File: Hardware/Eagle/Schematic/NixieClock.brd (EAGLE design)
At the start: 256.5 x 112.7 mm, 10 parts

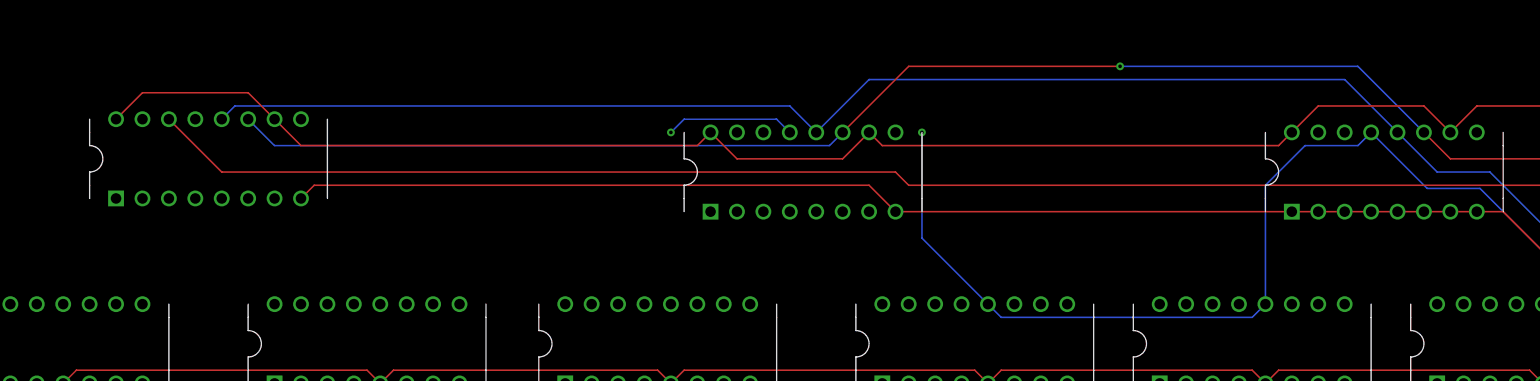
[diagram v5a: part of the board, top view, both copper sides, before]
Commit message: Schematic progress... chips in board layout are out of order.. fix later
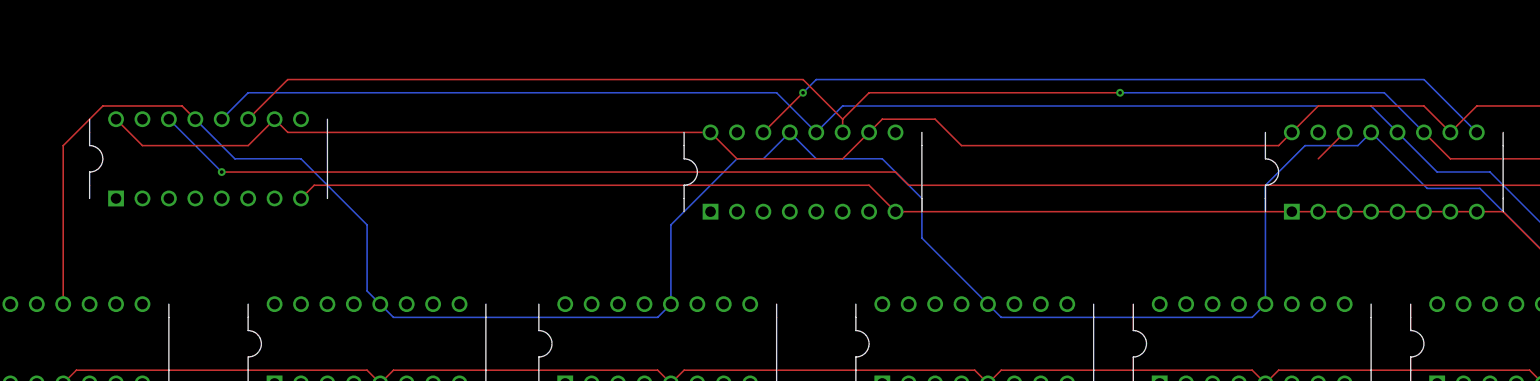
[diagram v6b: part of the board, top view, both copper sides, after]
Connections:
- new net N$7: U$2.P$9, U$3.P$14
- new net N$9: U$3.P$9, U$4.P$14
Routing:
- net N$1: track 156.7 -> 263.8 mm, vias 2 -> 0
- net N$9: track 0.00 -> 72.8 mm, vias 0 -> 1
- net N$7: track 0.00 -> 3.59 mm
- net N$5: track 169.1 -> 168.1 mm
- net N$3: vias 0 -> 1
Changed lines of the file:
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@@
 <wire x1="34.29" y1="43.18" x2="33.02" y2="44.45" width="0.1524" layer="16"/>
 <wire x1="33.02" y1="44.45" x2="26.67" y2="50.8" width="0.1524" layer="16"/>
-<wire x1="26.67" y1="50.8" x2="26.67" y2="60.96" width="0.1524" layer="16"/>
-<via x="26.67" y="60.96" extent="1-16" drill="0.35"/>
-<wire x1="13.97" y1="60.96" x2="12.7" y2="62.23" width="0.1524" layer="16"/>
-<wire x1="12.7" y1="62.23" x2="3.81" y2="62.23" width="0.1524" layer="16"/>
-<wire x1="3.81" y1="62.23" x2="2.54" y2="60.96" width="0.1524" layer="16"/>
-<via x="2.54" y="60.96" extent="1-16" drill="0.35"/>
-<wire x1="13.97" y1="60.96" x2="26.67" y2="60.96" width="0" layer="19" extent="1-1"/>
-<wire x1="2.54" y1="44.45" x2="2.54" y2="60.96" width="0" layer="19" extent="1-1"/>
-<wire x1="-25.4" y1="44.45" x2="2.54" y2="44.45" width="0" layer="19" extent="1-1"/>
-<wire x1="-43.18" y1="62.23" x2="-25.4" y2="44.45" width="0" layer="19" extent="1-1"/>
-<wire x1="-55.88" y1="44.45" x2="-43.18" y2="62.23" width="0" layer="19" extent="1-1"/>
+<wire x1="13.97" y1="60.96" x2="11.43" y2="58.42" width="0.1524" layer="16"/>
+<wire x1="11.43" y1="58.42" x2="8.89" y2="58.42" width="0.1524" layer="16"/>
+<wire x1="8.89" y1="58.42" x2="2.54" y2="52.07" width="0.1524" layer="16"/>
+<wire x1="2.54" y1="52.07" x2="2.54" y2="44.45" width="0.1524" layer="16"/>
+<wire x1="26.67" y1="50.8" x2="26.67" y2="54.61" width="0.1524" layer="16"/>
+<wire x1="26.67" y1="54.61" x2="22.86" y2="58.42" width="0.1524" layer="16"/>
+<wire x1="22.86" y1="58.42" x2="16.51" y2="58.42" width="0.1524" layer="16"/>
+<wire x1="16.51" y1="58.42" x2="13.97" y2="60.96" width="0.1524" layer="16"/>
+<wire x1="-43.18" y1="62.23" x2="-39.37" y2="58.42" width="0.1524" layer="16"/>
+<wire x1="-39.37" y1="58.42" x2="-33.02" y2="58.42" width="0.1524" layer="16"/>
+<wire x1="-33.02" y1="58.42" x2="-26.67" y2="52.07" width="0.1524" layer="16"/>
+<wire x1="-26.67" y1="52.07" x2="-26.67" y2="45.72" width="0.1524" layer="16"/>
+<wire x1="-26.67" y1="45.72" x2="-25.4" y2="44.45" width="0.1524" layer="16"/>
+<wire x1="-25.4" y1="44.45" x2="-24.13" y2="43.18" width="0.1524" layer="16"/>
+<wire x1="1.27" y1="43.18" x2="2.54" y2="44.45" width="0.1524" layer="16"/>
+<wire x1="-24.13" y1="43.18" x2="1.27" y2="43.18" width="0.1524" layer="16"/>
+<wire x1="-43.18" y1="62.23" x2="-44.45" y2="63.5" width="0.1524" layer="1"/>
+<wire x1="-44.45" y1="63.5" x2="-52.07" y2="63.5" width="0.1524" layer="1"/>
+<wire x1="-55.88" y1="59.69" x2="-55.88" y2="44.45" width="0.1524" layer="1"/>
+<wire x1="-52.07" y1="63.5" x2="-55.88" y2="59.69" width="0.1524" layer="1"/>
 </signal>
 <signal name="N$2">
@@
 <wire x1="64.77" y1="63.5" x2="62.23" y2="60.96" width="0.1524" layer="1"/>
 <wire x1="62.23" y1="60.96" x2="60.96" y2="59.69" width="0.1524" layer="1"/>
-<wire x1="60.96" y1="59.69" x2="22.86" y2="59.69" width="0.1524" layer="1"/>
-<wire x1="22.86" y1="59.69" x2="21.59" y2="60.96" width="0.1524" layer="1"/>
-<wire x1="6.35" y1="60.96" x2="5.08" y2="59.69" width="0.1524" layer="1"/>
-<wire x1="5.08" y1="59.69" x2="-33.02" y2="59.69" width="0.1524" layer="1"/>
-<wire x1="-33.02" y1="59.69" x2="-35.56" y2="62.23" width="0.1524" layer="1"/>
-<wire x1="-35.56" y1="62.23" x2="-38.1" y2="64.77" width="0.1524" layer="1"/>
-<wire x1="-38.1" y1="64.77" x2="-48.26" y2="64.77" width="0.1524" layer="1"/>
-<wire x1="-48.26" y1="64.77" x2="-50.8" y2="62.23" width="0.1524" layer="1"/>
+<wire x1="60.96" y1="59.69" x2="30.48" y2="59.69" width="0.1524" layer="1"/>
+<wire x1="30.48" y1="59.69" x2="27.94" y2="62.23" width="0.1524" layer="1"/>
+<wire x1="27.94" y1="62.23" x2="22.86" y2="62.23" width="0.1524" layer="1"/>
+<wire x1="22.86" y1="62.23" x2="21.59" y2="60.96" width="0.1524" layer="1"/>
+<wire x1="6.35" y1="60.96" x2="-34.29" y2="60.96" width="0.1524" layer="1"/>
+<wire x1="-34.29" y1="60.96" x2="-35.56" y2="62.23" width="0.1524" layer="1"/>
+<wire x1="-35.56" y1="62.23" x2="-38.1" y2="59.69" width="0.1524" layer="1"/>
+<wire x1="-50.8" y1="62.23" x2="-48.26" y2="59.69" width="0.1524" layer="1"/>
+<wire x1="-38.1" y1="59.69" x2="-48.26" y2="59.69" width="0.1524" layer="1"/>
 <wire x1="6.35" y1="60.96" x2="8.89" y2="58.42" width="0.1524" layer="1"/>
 <wire x1="21.59" y1="60.96" x2="19.05" y2="58.42" width="0.1524" layer="1"/>
@@
 <wire x1="25.401325" y1="55.878675" x2="24.13" y2="57.15" width="0.1524" layer="1"/>
 <wire x1="24.13" y1="57.15" x2="-40.64" y2="57.15" width="0.1524" layer="1"/>
-<wire x1="-40.64" y1="57.15" x2="-45.72" y2="62.23" width="0.1524" layer="1"/>
 <wire x1="86.361325" y1="55.878675" x2="87.7822" y2="54.4578" width="0.1524" layer="1"/>
 <wire x1="87.7822" y1="54.4578" x2="110.3378" y2="54.4578" width="0.1524" layer="1"/>
+<via x="-40.64" y="57.15" extent="1-16" drill="0.35"/>
+<wire x1="-40.64" y1="57.15" x2="-45.72" y2="62.23" width="0.1524" layer="16"/>
 </signal>
 <signal name="N$4">
@@
 <wire x1="86.36" y1="58.42" x2="77.47" y2="58.42" width="0.1524" layer="1"/>
 <wire x1="77.47" y1="58.42" x2="74.93" y2="60.96" width="0.1524" layer="1"/>
-<wire x1="74.93" y1="60.96" x2="68.58" y2="67.31" width="0.1524" layer="16"/>
-<wire x1="68.58" y1="67.31" x2="45.72" y2="67.31" width="0.1524" layer="16"/>
-<wire x1="19.05" y1="60.96" x2="17.78" y2="59.69" width="0.1524" layer="16"/>
-<wire x1="-38.1" y1="62.23" x2="-35.56" y2="59.69" width="0.1524" layer="16"/>
-<wire x1="17.78" y1="59.69" x2="-35.56" y2="59.69" width="0.1524" layer="16"/>
-<via x="45.72" y="67.31" extent="1-16" drill="0.35"/>
-<wire x1="45.72" y1="67.31" x2="25.4" y2="67.31" width="0.1524" layer="1"/>
-<wire x1="25.4" y1="67.31" x2="19.05" y2="60.96" width="0.1524" layer="1"/>
+<wire x1="74.93" y1="60.96" x2="71.12" y2="64.77" width="0.1524" layer="16"/>
+<wire x1="71.12" y1="64.77" x2="45.72" y2="64.77" width="0.1524" layer="16"/>
+<via x="45.72" y="64.77" extent="1-16" drill="0.35"/>
+<wire x1="45.72" y1="64.77" x2="21.59" y2="64.77" width="0.1524" layer="1"/>
+<wire x1="21.59" y1="64.77" x2="19.05" y2="62.23" width="0.1524" layer="1"/>
+<wire x1="19.05" y1="60.96" x2="19.05" y2="62.23" width="0.1524" layer="1"/>
+<wire x1="19.05" y1="62.23" x2="15.24" y2="66.04" width="0.1524" layer="1"/>
+<wire x1="-34.29" y1="66.04" x2="15.24" y2="66.04" width="0.1524" layer="1"/>
+<wire x1="-38.1" y1="62.23" x2="-34.29" y2="66.04" width="0.1524" layer="1"/>
 </signal>
 <signal name="N$5">
@@
 <wire x1="81.28" y1="57.15" x2="76.2" y2="57.15" width="0.1524" layer="16"/>
 <wire x1="76.2" y1="57.15" x2="72.39" y2="60.96" width="0.1524" layer="16"/>
-<wire x1="72.39" y1="60.96" x2="67.31" y2="66.04" width="0.1524" layer="16"/>
-<wire x1="21.59" y1="66.04" x2="16.51" y2="60.96" width="0.1524" layer="16"/>
-<wire x1="67.31" y1="66.04" x2="21.59" y2="66.04" width="0.1524" layer="16"/>
-<wire x1="-40.64" y1="62.23" x2="-39.37" y2="63.5" width="0.1524" layer="16"/>
-<wire x1="16.51" y1="60.96" x2="13.97" y2="63.5" width="0.1524" layer="16"/>
-<wire x1="13.97" y1="63.5" x2="-39.37" y2="63.5" width="0.1524" layer="16"/>
+<wire x1="72.39" y1="60.96" x2="69.85" y2="63.5" width="0.1524" layer="16"/>
+<wire x1="19.05" y1="63.5" x2="16.51" y2="60.96" width="0.1524" layer="16"/>
+<wire x1="69.85" y1="63.5" x2="19.05" y2="63.5" width="0.1524" layer="16"/>
+<wire x1="-40.64" y1="62.23" x2="-38.1" y2="64.77" width="0.1524" layer="16"/>
+<wire x1="16.51" y1="60.96" x2="12.7" y2="64.77" width="0.1524" layer="16"/>
+<wire x1="12.7" y1="64.77" x2="-38.1" y2="64.77" width="0.1524" layer="16"/>
 </signal>
 <signal name="N$6">
@@
 <wire x1="-54.61" y1="38.1" x2="-55.88" y2="36.83" width="0.1524" layer="1"/>
 </signal>
+<signal name="N$7">
+<contactref element="U$2" pad="P$9"/>
+<contactref element="U$3" pad="P$14"/>
+<wire x1="67.31" y1="60.96" x2="64.77" y2="58.42" width="0.1524" layer="1"/>
+<wire x1="-33.02" y1="62.23" x2="64.77" y2="58.42" width="0" layer="19" extent="1-1"/>
+</signal>
+<signal name="N$9">
+<contactref element="U$3" pad="P$9"/>
+<contactref element="U$4" pad="P$14"/>
+<wire x1="80.01" y1="60.96" x2="74.93" y2="66.04" width="0.1524" layer="16"/>
+<wire x1="16.51" y1="66.04" x2="15.24" y2="64.77" width="0.1524" layer="16"/>
+<wire x1="74.93" y1="66.04" x2="16.51" y2="66.04" width="0.1524" layer="16"/>
+<via x="15.24" y="64.77" extent="1-16" drill="0.35"/>
+<wire x1="15.24" y1="64.77" x2="11.43" y2="60.96" width="0.1524" layer="1"/>
+</signal>
 </signals>

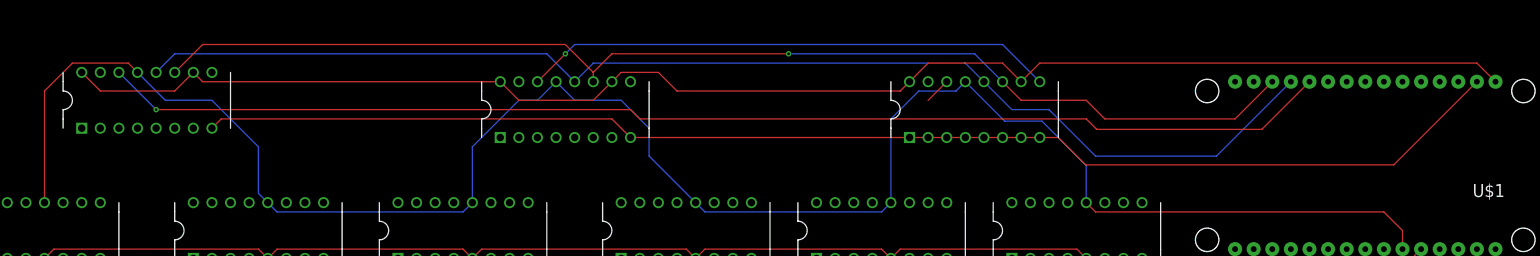
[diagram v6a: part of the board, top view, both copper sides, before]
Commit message: Chips in board layout in correct order
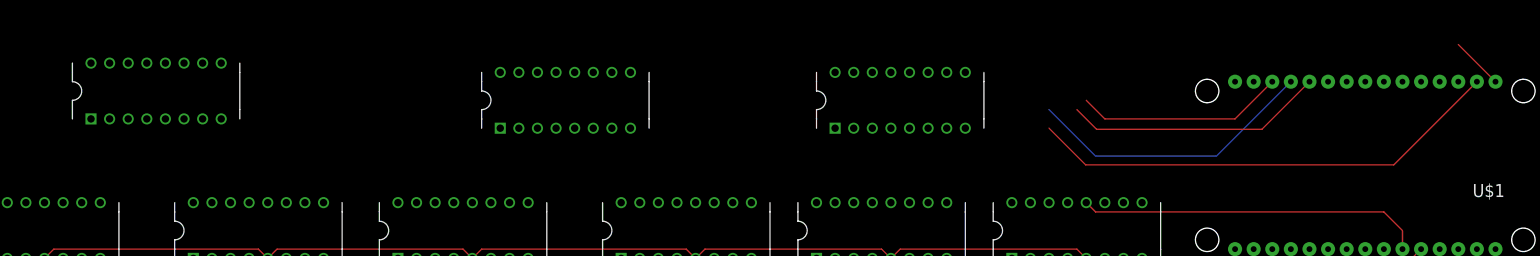
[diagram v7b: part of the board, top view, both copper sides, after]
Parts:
- moved U$2 102.9 mm to (61.0, 58.4)
- moved U$4 55.9 mm to (-40.6, 59.7)
- moved U$3 55.9 mm to (15.2, 58.4)
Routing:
- net N$1: track 263.8 -> 47.3 mm
- net N$2: track 204.1 -> 7.18 mm
- net N$3: track 168.5 -> 35.6 mm, vias 1 -> 0
- net N$4: track 161.1 -> 28.6 mm, vias 1 -> 0
- net N$5: track 168.1 -> 39.9 mm
- net N$6: track 180.5 -> 65.2 mm
- net N$9: track 72.8 -> 0.00 mm, vias 1 -> 0
- net N$7: track 3.59 -> 0.00 mm

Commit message: All wires from shift registers to nixie driver inputs routed
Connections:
- new net N$10: U$10.P$3, U$2.P$7
- new net N$11: U$3.P$7, U$8.P$3
- new net N$12: U$4.P$7, U$6.P$3
- new net N$13: U$10.P$6, U$2.P$6
- new net N$14: U$3.P$6, U$8.P$6
- new net N$15: U$4.P$6, U$6.P$6
- new net N$16: U$10.P$7, U$2.P$5
- new net N$17: U$3.P$5, U$8.P$7
- new net N$18: U$4.P$5, U$6.P$7
- new net N$19: U$10.P$4, U$2.P$4
- new net N$20: U$3.P$4, U$8.P$4
- new net N$21: U$4.P$4, U$6.P$4
- new net N$22: U$2.P$3, U$9.P$3
- new net N$23: U$3.P$3, U$7.P$3
- new net N$24: U$4.P$3, U$5.P$3
- new net N$25: U$2.P$2, U$9.P$6
- new net N$26: U$3.P$2, U$7.P$6
- new net N$27: U$4.P$2, U$5.P$6
- new net N$28: U$2.P$1, U$9.P$7
- new net N$29: U$3.P$1, U$7.P$7
- new net N$30: U$4.P$1, U$5.P$7
- new net N$31: U$4.P$15, U$5.P$4
- new net N$32: U$3.P$15, U$7.P$4
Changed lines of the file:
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@@
 <wire x1="-44.45" y1="63.5" x2="24.13" y2="62.23" width="0" layer="19" extent="1-1"/>
+</signal>
+<signal name="N$10">
+<contactref element="U$2" pad="P$7"/>
+<contactref element="U$10" pad="P$3"/>
+<wire x1="81.28" y1="36.83" x2="67.31" y2="54.61" width="0" layer="19" extent="1-1"/>
+</signal>
+<signal name="N$11">
+<contactref element="U$3" pad="P$7"/>
+<contactref element="U$8" pad="P$3"/>
+<wire x1="27.94" y1="36.83" x2="21.59" y2="54.61" width="0" layer="19" extent="1-1"/>
+</signal>
+<signal name="N$12">
+<contactref element="U$4" pad="P$7"/>
+<contactref element="U$6" pad="P$3"/>
+<wire x1="-30.48" y1="36.83" x2="-34.29" y2="55.88" width="0" layer="19" extent="1-1"/>
+</signal>
+<signal name="N$13">
+<contactref element="U$2" pad="P$6"/>
+<contactref element="U$10" pad="P$6"/>
+<wire x1="64.77" y1="54.61" x2="88.9" y2="36.83" width="0" layer="19" extent="1-1"/>
+</signal>
+<signal name="N$14">
+<contactref element="U$3" pad="P$6"/>
+<contactref element="U$8" pad="P$6"/>
+<wire x1="35.56" y1="36.83" x2="19.05" y2="54.61" width="0" layer="19" extent="1-1"/>
+</signal>
+<signal name="N$15">
+<contactref element="U$4" pad="P$6"/>
+<contactref element="U$6" pad="P$6"/>
+<wire x1="-22.86" y1="36.83" x2="-36.83" y2="55.88" width="0" layer="19" extent="1-1"/>
+</signal>
+<signal name="N$16">
+<contactref element="U$2" pad="P$5"/>
+<contactref element="U$10" pad="P$7"/>
+<wire x1="62.23" y1="54.61" x2="91.44" y2="36.83" width="0" layer="19" extent="1-1"/>
+</signal>
+<signal name="N$17">
+<contactref element="U$3" pad="P$5"/>
+<contactref element="U$8" pad="P$7"/>
+<wire x1="16.51" y1="54.61" x2="38.1" y2="36.83" width="0" layer="19" extent="1-1"/>
+</signal>
+<signal name="N$18">
+<contactref element="U$4" pad="P$5"/>
+<contactref element="U$6" pad="P$7"/>
+<wire x1="-20.32" y1="36.83" x2="-39.37" y2="55.88" width="0" layer="19" extent="1-1"/>
+</signal>
+<signal name="N$19">
+<contactref element="U$2" pad="P$4"/>
+<contactref element="U$10" pad="P$4"/>
+<wire x1="59.69" y1="54.61" x2="83.82" y2="36.83" width="0" layer="19" extent="1-1"/>
+</signal>
+<signal name="N$20">
+<contactref element="U$3" pad="P$4"/>
+<contactref element="U$8" pad="P$4"/>
+<wire x1="30.48" y1="36.83" x2="13.97" y2="54.61" width="0" layer="19" extent="1-1"/>
+</signal>
+<signal name="N$21">
+<contactref element="U$4" pad="P$4"/>
+<contactref element="U$6" pad="P$4"/>
+<wire x1="-27.94" y1="36.83" x2="-41.91" y2="55.88" width="0" layer="19" extent="1-1"/>
+</signal>
+<signal name="N$22">
+<contactref element="U$2" pad="P$3"/>
+<contactref element="U$9" pad="P$3"/>
+<wire x1="54.61" y1="36.83" x2="57.15" y2="54.61" width="0" layer="19" extent="1-1"/>
+</signal>
+<signal name="N$23">
+<contactref element="U$3" pad="P$3"/>
+<contactref element="U$7" pad="P$3"/>
+<wire x1="-2.54" y1="36.83" x2="11.43" y2="54.61" width="0" layer="19" extent="1-1"/>
+</signal>
+<signal name="N$24">
+<contactref element="U$4" pad="P$3"/>
+<contactref element="U$5" pad="P$3"/>
+<wire x1="-44.45" y1="55.88" x2="-60.96" y2="36.83" width="0" layer="19" extent="1-1"/>
+</signal>
+<signal name="N$25">
+<contactref element="U$2" pad="P$2"/>
+<contactref element="U$9" pad="P$6"/>
+<wire x1="62.23" y1="36.83" x2="54.61" y2="54.61" width="0" layer="19" extent="1-1"/>
+</signal>
+<signal name="N$26">
+<contactref element="U$3" pad="P$2"/>
+<contactref element="U$7" pad="P$6"/>
+<wire x1="5.08" y1="36.83" x2="8.89" y2="54.61" width="0" layer="19" extent="1-1"/>
+</signal>
+<signal name="N$27">
+<contactref element="U$4" pad="P$2"/>
+<contactref element="U$5" pad="P$6"/>
+<wire x1="-46.99" y1="55.88" x2="-53.34" y2="36.83" width="0" layer="19" extent="1-1"/>
+</signal>
+<signal name="N$28">
+<contactref element="U$2" pad="P$1"/>
+<contactref element="U$9" pad="P$7"/>
+<wire x1="64.77" y1="36.83" x2="52.07" y2="54.61" width="0" layer="19" extent="1-1"/>
+</signal>
+<signal name="N$29">
+<contactref element="U$3" pad="P$1"/>
+<contactref element="U$7" pad="P$7"/>
+<wire x1="7.62" y1="36.83" x2="6.35" y2="54.61" width="0" layer="19" extent="1-1"/>
+</signal>
+<signal name="N$30">
+<contactref element="U$4" pad="P$1"/>
+<contactref element="U$5" pad="P$7"/>
+<wire x1="-49.53" y1="55.88" x2="-50.8" y2="36.83" width="0" layer="19" extent="1-1"/>
+</signal>
+<signal name="N$31">
+<contactref element="U$5" pad="P$4"/>
+<contactref element="U$4" pad="P$15"/>
+<wire x1="-46.99" y1="63.5" x2="-58.42" y2="36.83" width="0" layer="19" extent="1-1"/>
+</signal>
+<signal name="N$32">
+<contactref element="U$3" pad="P$15"/>
+<contactref element="U$7" pad="P$4"/>
+<wire x1="0" y1="36.83" x2="8.89" y2="62.23" width="0" layer="19" extent="1-1"/>
 </signal>
 </signals>
